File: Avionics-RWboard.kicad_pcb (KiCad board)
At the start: 4 copper layers, 73.3 x 54.2 mm, 41 parts, among them J1 282834-2, J3 Screw_Terminal_01x03, U1 MCF8315C1VQRGFRQ1

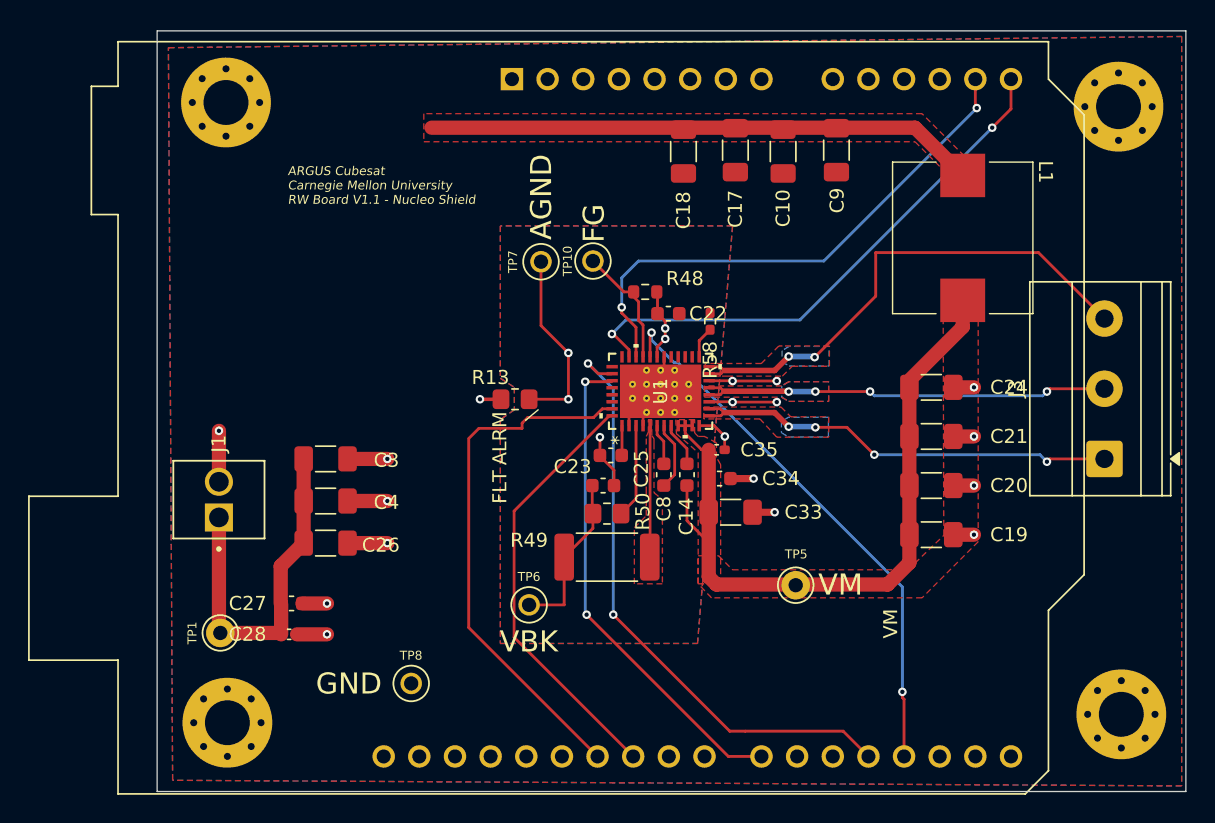
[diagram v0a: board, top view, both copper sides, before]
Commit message: moved inductor and added leds
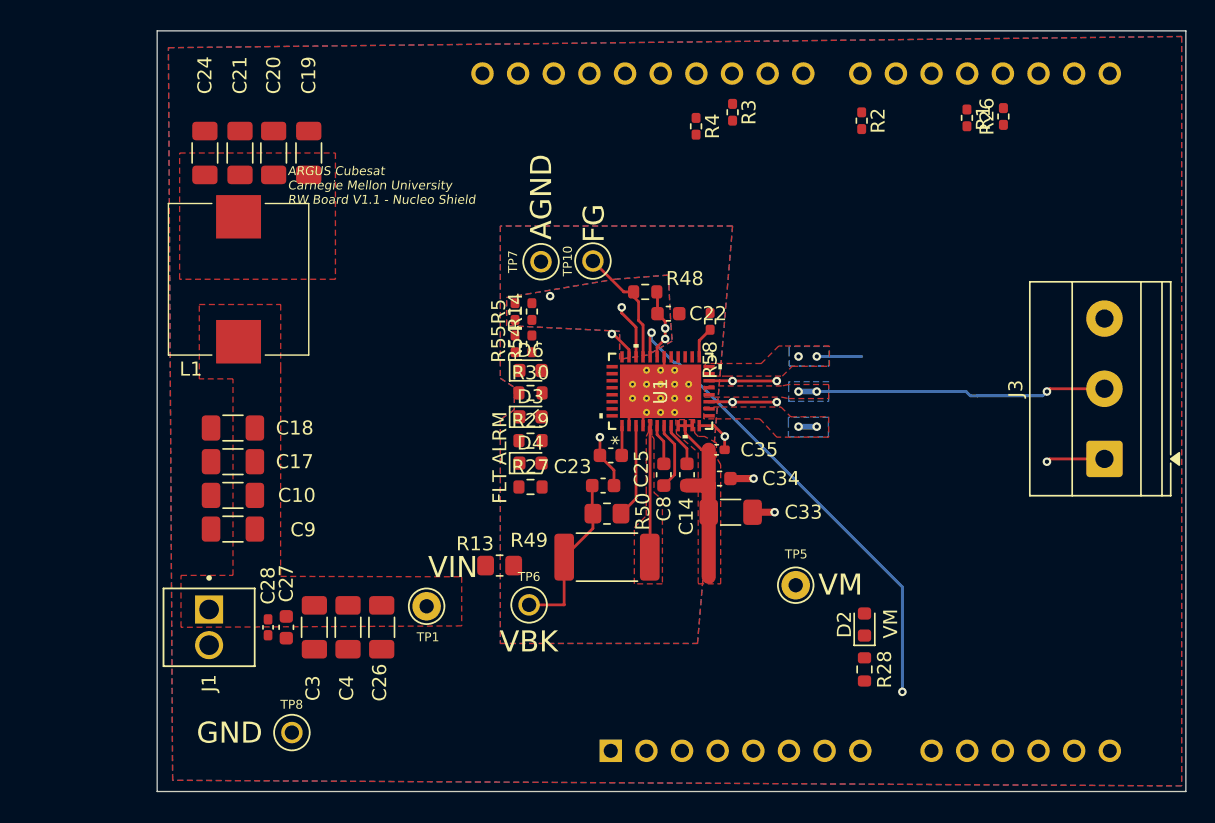
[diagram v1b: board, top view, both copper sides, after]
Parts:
- removed H1, H2, H3, H4: MountingHole_Pad, MountingHole:MountingHole_3.2mm_M3_Pad_Via
- added D2: GREEN LED, LED_SMD:LED_0603_1608Metric, F.Cu at (162.9, 112.4)
- added D3: RED LED, LED_SMD:LED_0603_1608Metric, F.Cu at (139.1, 97.6)
- added D4: GREEN LED, LED_SMD:LED_0603_1608Metric, F.Cu at (139.1, 100.9)
- added D6: RED LED, LED_SMD:LED_0603_1608Metric, F.Cu at (139.1, 94.3)
- added R1: 0R, Resistor_SMD:R_0402_1005Metric_Pad0.72x0.64mm_HandSolder, F.Cu at (170.2, 76.3)
- added R14: 0R, Resistor_SMD:R_0402_1005Metric_Pad0.72x0.64mm_HandSolder, F.Cu at (139.2, 90.1)
- added R2: 0R, Resistor_SMD:R_0402_1005Metric_Pad0.72x0.64mm_HandSolder, F.Cu at (162.7, 76.5)
- added R26: 0R, Resistor_SMD:R_0402_1005Metric_Pad0.72x0.64mm_HandSolder, F.Cu at (172.8, 76.2)
- added R27: 1k, Resistor_SMD:R_0603_1608Metric, F.Cu at (139.1, 102.6)
- added R28: 4k7, Resistor_SMD:R_0603_1608Metric, F.Cu at (162.9, 115.6)
- added R29: 1k, Resistor_SMD:R_0603_1608Metric, F.Cu at (139.1, 99.3)
- added R3: 0R, Resistor_SMD:R_0402_1005Metric_Pad0.72x0.64mm_HandSolder, F.Cu at (153.5, 75.9)
- added R30: 470R, Resistor_SMD:R_0603_1608Metric, F.Cu at (139.1, 95.9)
- added R4: 0R, Resistor_SMD:R_0402_1005Metric_Pad0.72x0.64mm_HandSolder, F.Cu at (150.9, 76.9)
- added R5: 0R, Resistor_SMD:R_0402_1005Metric_Pad0.72x0.64mm_HandSolder, F.Cu at (138.0, 90.1)
- added R54: 0R, Resistor_SMD:R_0402_1005Metric_Pad0.72x0.64mm_HandSolder, F.Cu at (139.2, 92.4)
- added R55: 0R, Resistor_SMD:R_0402_1005Metric_Pad0.72x0.64mm_HandSolder, F.Cu at (138.0, 92.4)
- A1: moved to B.Cu
- moved C24 54.4 mm to (115.9, 78.8), turned to -90 degrees
- moved C21 53.2 mm to (118.4, 78.8), turned to -90 degrees
- moved C20 52.5 mm to (120.8, 78.8), turned to -90 degrees
- moved C19 52.0 mm to (123.3, 78.8), turned to -90 degrees
- moved L1 51.7 mm to (118.3, 87.8), turned to 90 degrees
- moved C9 50.8 mm to (117.9, 105.6), turned to 0 degrees
- moved A1 48.4 mm to (144.8, 121.4)
- moved C10 46.2 mm to (117.9, 103.2), turned to 0 degrees
- moved C17 42.1 mm to (117.9, 100.8), turned to 0 degrees
- moved C18 37.7 mm to (117.9, 98.4), turned to 0 degrees
- moved TP1 14.8 mm to (131.7, 111.1)
- moved C3 12.0 mm to (123.7, 112.6), turned to 90 degrees
- moved R13 11.9 mm to (136.9, 108.2)
- moved TP8 9.19 mm to (122.1, 120.1)
- moved C4 9.14 mm to (126.1, 112.6), turned to 90 degrees
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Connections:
- A1 pad 18: /Connectors/SPEED_WAKE -> Net-(A1-D3)
- A1 pad 19: /Connectors/DIR -> Net-(A1-D4)
- A1 pad 22: /Connectors/BRAKE -> Net-(A1-D7)
- A1 pad 25: /Connectors/RW_MOTOR_FLT -> Net-(A1-D10)
- A1 pad 26: /Connectors/RW_MOTOR_ALRM -> Net-(A1-D11)
- C10 pad 2: /Power/VMAIN -> VIN
- C17 pad 2: /Power/VMAIN -> VIN
- C18 pad 2: /Power/VMAIN -> VIN
- C26 pad 2: VMAIN -> VIN
- C27 pad 2: VMAIN -> VIN
- C28 pad 2: VMAIN -> VIN
- C3 pad 2: VMAIN -> VIN
- C4 pad 2: VMAIN -> VIN
- C9 pad 2: /Power/VMAIN -> VIN
- J1 pad 1: VMAIN -> VIN
- L1 pad 1: /Power/VMAIN -> VIN
- TP1 pad TP: VMAIN -> VIN
- U1 pad 34: /Connectors/DIR -> /Motor/DIR
- U1 pad 35: /Connectors/BRAKE -> /Motor/BRAKE
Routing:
- net VM: track 59.5 -> 14.3 mm
- net /Connectors/DIR: track 43.0 -> 0.00 mm, vias 2 -> 0
- net /Power/VMAIN: track 39.3 -> 0.00 mm
- net /Connectors/RW_MOTOR_ALRM: track 37.8 -> 0.00 mm
- net /Connectors/SCL: track 39.4 -> 2.19 mm, vias 2 -> 1
- net /Connectors/BRAKE: track 35.2 -> 0.00 mm, vias 2 -> 0
- net /Connectors/SDA: track 38.5 -> 3.95 mm, vias 2 -> 1
- net Net-(J3-Pin_3): track 36.7 -> 3.20 mm
- net /Connectors/RW_MOTOR_FLT: track 30.8 -> 0.00 mm
- net VMAIN: track 26.0 -> 0.00 mm
- net Net-(J3-Pin_1): track 30.9 -> 5.49 mm, vias 4 -> 3
- net GND: track 39.5 -> 16.1 mm, vias 18 -> 7
- net AGND: track 27.4 -> 14.0 mm, vias 3 -> 1
- net Net-(J3-Pin_2): track 29.7 -> 22.0 mm, vias 4 -> 3
- net /Connectors/SPEED_WAKE: track 39.6 -> 34.9 mm
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- added copper zone on B.Cu, net AVDD
- added copper zone on F.Cu, net AVDD
- added copper zone on F.Cu, net VIN
- removed copper zone on In2.Cu, net (none)
- removed copper zone on F.Cu, net /Power/VMAIN
- removed copper zone on In2.Cu, net AVDD
- removed copper zone on In2.Cu, net GND
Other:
- board text added: "VIN"

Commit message: finished board
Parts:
- added R6: 4.7k, Resistor_SMD:R_0603_1608Metric, F.Cu at (168.1, 115.8)
- added R7: 4.7k, Resistor_SMD:R_0603_1608Metric, F.Cu at (168.1, 112.5)
- C28, C35: footprint Capacitor_SMD:C_0402_1005Metric_Pad0.74x0.62mm_HandSolder -> Capacitor_SMD:C_0603_1608Metric
- R1, R14, R2, R26, R3, R4, R5, R54, R55, R58: footprint Resistor_SMD:R_0402_1005Metric_Pad0.72x0.64mm_HandSolder -> Resistor_SMD:R_0603_1608Metric
- moved C24 39.9 mm to (125.2, 117.6), turned to 90 degrees
- moved C19 39.2 mm to (117.8, 117.6), turned to 90 degrees
- moved C21 39.0 mm to (122.7, 117.6), turned to 90 degrees
- moved C20 38.8 mm to (120.3, 117.6), turned to 90 degrees
- moved J1 31.0 mm to (116.5, 81.6), turned to 90 degrees
- moved C26 30.8 mm to (129.3, 81.8), turned to -90 degrees
- moved C27 30.8 mm to (122.5, 81.8), turned to -90 degrees
- moved C3 30.8 mm to (124.5, 81.8), turned to -90 degrees
- moved C4 30.8 mm to (126.9, 81.8), turned to -90 degrees
- moved C28 30.8 mm to (120.9, 81.8), turned to -90 degrees
- moved TP8 30.0 mm to (127.2, 90.5)
- moved TP1 27.7 mm to (132.3, 83.4)
- moved L1 20.3 mm to (118.8, 108.1), turned to -90 degrees
- moved R27 11.4 mm to (146.8, 111.0)
- moved D4 11.0 mm to (143.5, 111.0), turned to 180 degrees
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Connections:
- A1 pad 4: unconnected-(A1-3V3-Pad4) -> 3V3
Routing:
- net /Connectors/SDA: track 3.95 -> 57.4 mm, vias 1 -> 2
- net /Connectors/SCL: track 2.19 -> 55.5 mm, vias 1 -> 2
- net /Connectors/RW_MOTOR_FLT: track 0.00 -> 40.6 mm, vias 0 -> 2
- net /Motor/BRAKE: track 0.00 -> 36.9 mm, vias 0 -> 2
- net /Motor/DIR: track 0.00 -> 34.5 mm, vias 0 -> 2
- net /Connectors/RW_MOTOR_ALRM: track 0.00 -> 32.8 mm, vias 0 -> 2
- net 3V3: track 0.00 -> 20.5 mm
- net VM: track 14.3 -> 34.7 mm
- net Net-(J3-Pin_3): track 3.20 -> 21.5 mm, vias 2 -> 0
- net Net-(J3-Pin_1): track 5.49 -> 21.3 mm, vias 3 -> 0
- net Net-(A1-D4): track 0.00 -> 11.9 mm
- net Net-(A1-D3): track 0.00 -> 11.2 mm
- net /Connectors/SPEED_WAKE: track 34.9 -> 24.5 mm
- net /Motor/SW_BUCK: track 9.38 -> 0.00 mm
- net Net-(A1-D7): track 0.00 -> 7.44 mm
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- added copper zone on In2.Cu, net GND
- removed copper zone on B.Cu, net AGND
- removed copper zone on In1.Cu, net AGND
- removed copper zone on In2.Cu, net AGND
- removed copper zone on B.Cu, net AVDD
- removed copper zone on B.Cu, net Net-(J3-Pin_1)
- removed copper zone on B.Cu, net Net-(J3-Pin_2)
- removed copper zone on B.Cu, net Net-(J3-Pin_3)

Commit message: finished board
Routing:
- removed copper zone on In1.Cu, net GND
- removed copper zone on In2.Cu, net GND
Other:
- copper layers 4 -> 2
- board text added: "+"
- board text added: "-"
- board text added: "ARGUS 3 Cubesat Carnegie Mellon University RW Nucleo Shield V1.0"
- board text removed: "ARGUS Cubesat Carnegie Mellon University RW Board V1.1 - Nucleo Shield"
